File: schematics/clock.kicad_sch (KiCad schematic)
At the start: 20 parts, among them Q11 DTC014T_SOT-416, U32 NB3L202KMN, U33 SN65LVDS1_SOIC, U34 Oscillator_27MHz_JU6, Y4 Oscillator_100MHz_NX324, Y5 Oscillator_26MHz_ESC_2520MV, Y6 Oscillator_125MHz_AX3DA

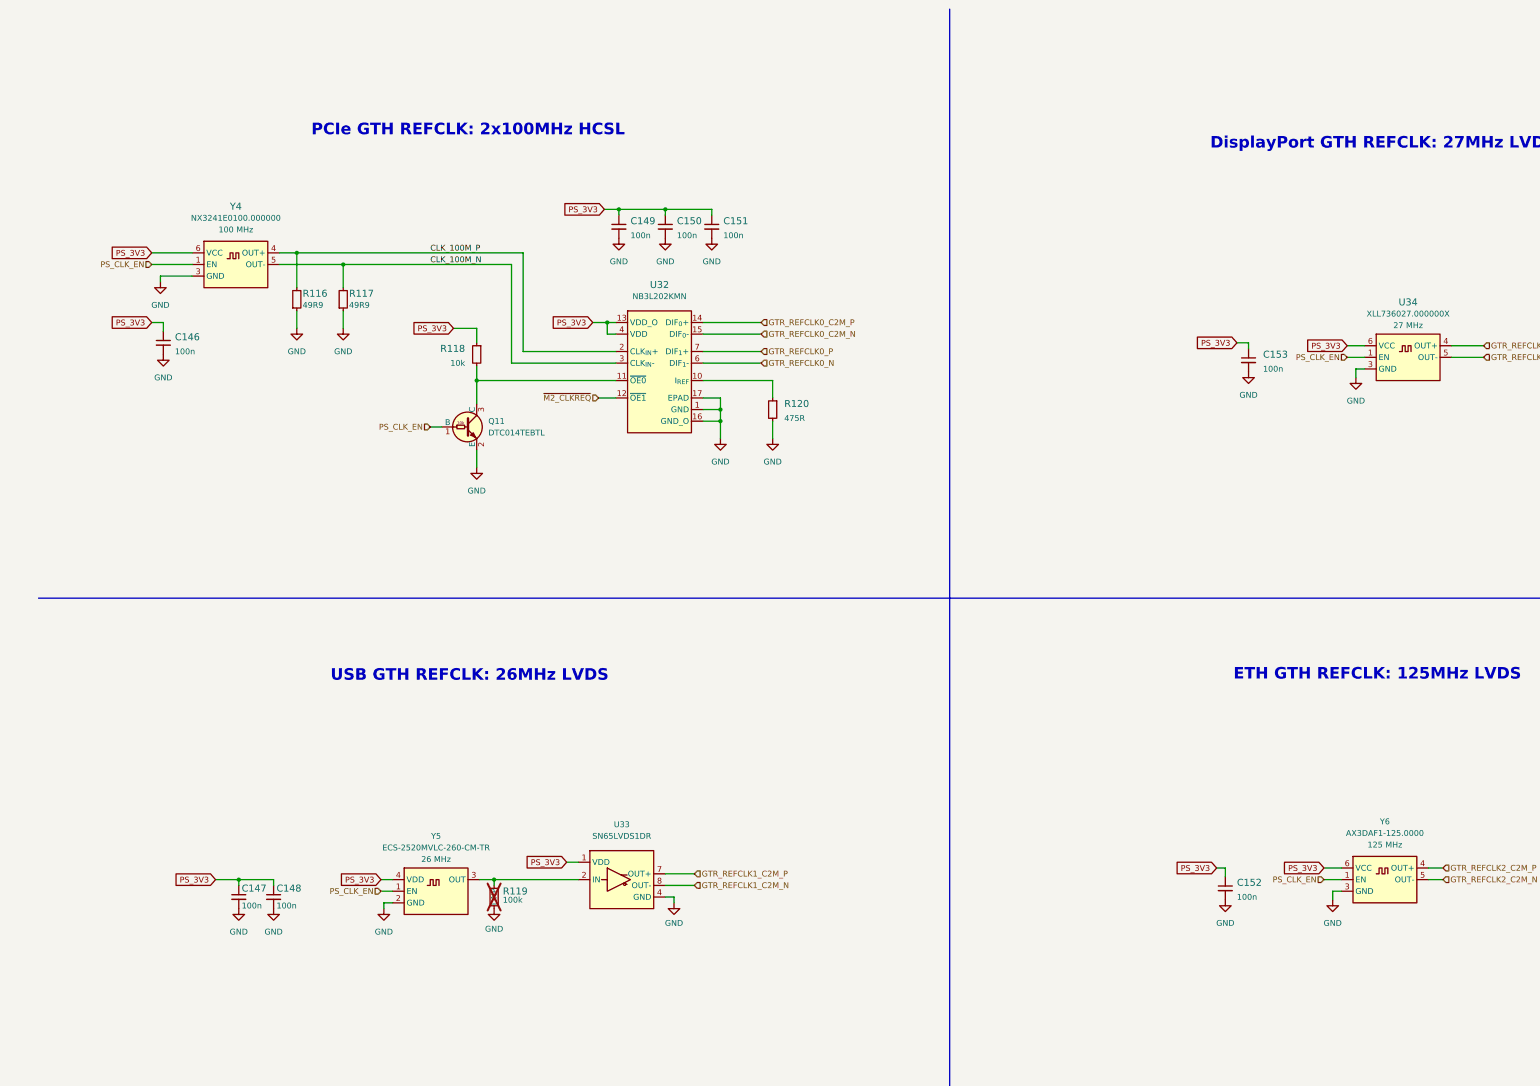
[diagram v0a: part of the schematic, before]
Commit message: Voltage converter added
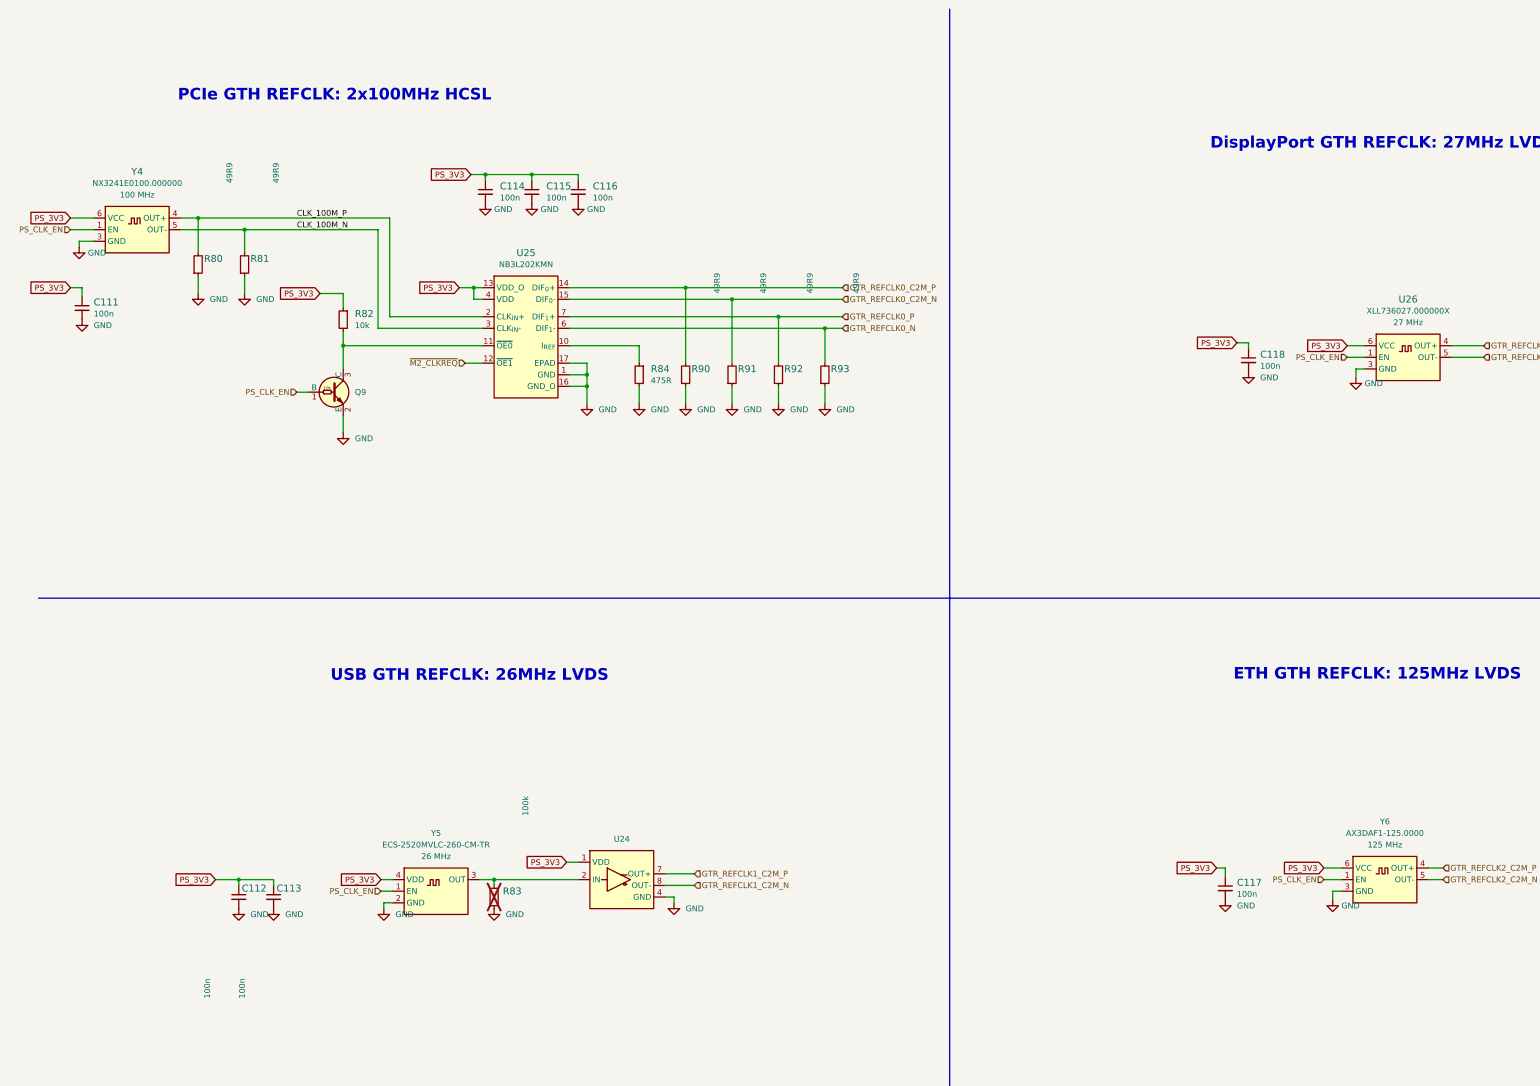
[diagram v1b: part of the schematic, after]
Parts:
- added R90, R91, R92, R93: R_49R9_0402, kria-k26-devboard-footprints:R_0402_1005Metric, symbol kria-k26-devboard:R_49R9_0402
- R83: renamed from R119; DNP DNP -> (none); now in the parts list
- renumbered C146 to C111, C147 to C112, C148 to C113, C149 to C114, C150 to C115, C151 to C116, C152 to C117, C153 to C118, Q11 to Q9, R116 to R80, R117 to R81, R118 to R82, R120 to R84, U33 to U24, U32 to U25, U34 to U26
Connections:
- net GND: now also R90.1, R91.1, R92.1, R93.1
- net GTR_REFCLK0_C2M_N: now also R91.2
- net GTR_REFCLK0_C2M_P: now also R90.2
- net GTR_REFCLK0_N: now also R93.2
- net GTR_REFCLK0_P: now also R92.2
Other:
- moved on the sheet: C111, C114, C115, C116, Q9, R80, R81, R82, R84, U25, Y4
